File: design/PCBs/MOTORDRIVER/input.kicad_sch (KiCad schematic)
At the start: 2 parts, among them J1 Screw_Terminal_01x02, P3 USB_C_Plug_USB2.0

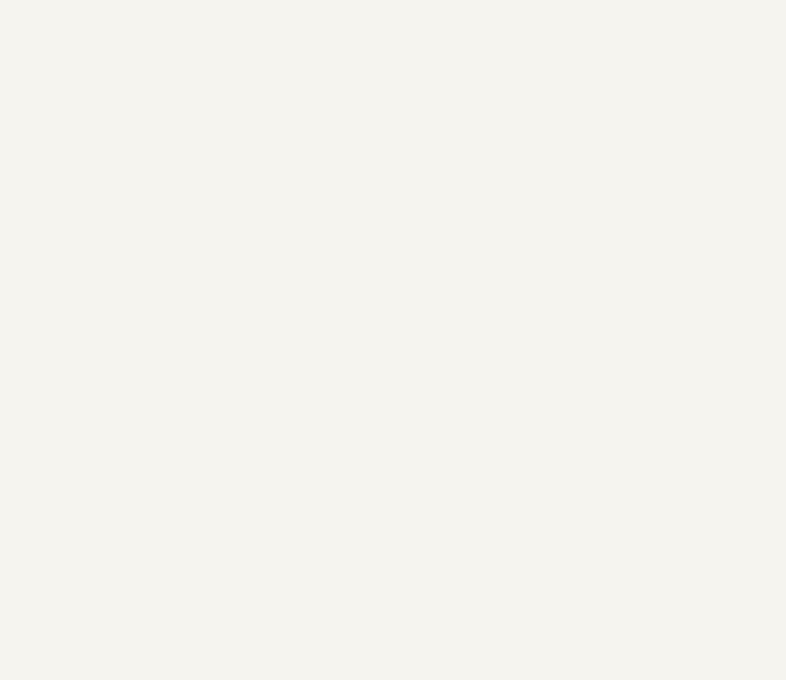
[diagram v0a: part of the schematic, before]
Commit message: Added micro-servo headers Added header for FFC cable IMU PCB
We need to set IMU PCB input to correspond to
the one we have made here.
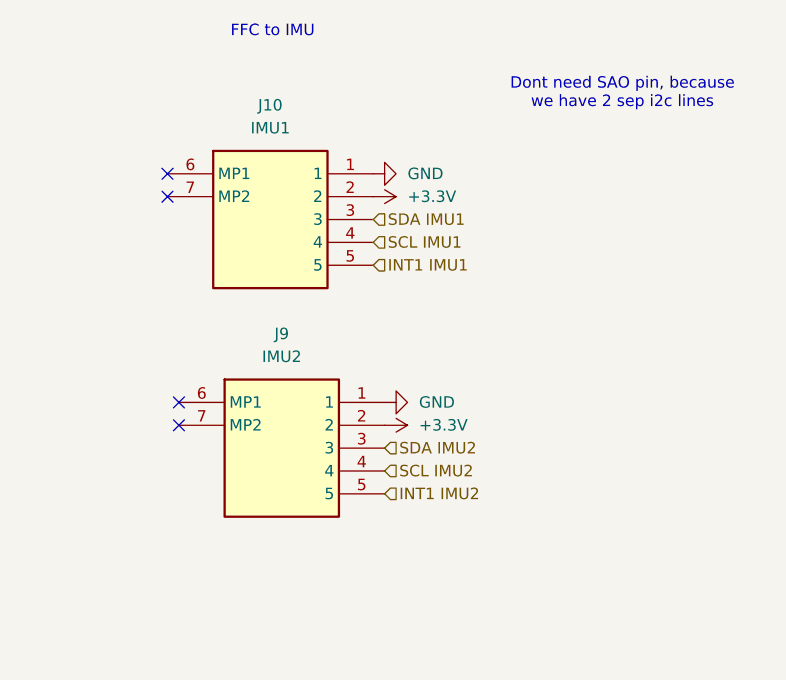
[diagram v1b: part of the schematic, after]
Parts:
- added J10: IMU1, 59453052110ECHLF, symbol 59453-052110ECHLF:59453-052110ECHLF
- added J9: IMU2, 59453052110ECHLF, symbol 59453-052110ECHLF:59453-052110ECHLF
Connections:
- net GND: now also J10.1, J9.1
- new net +3.3V: J10.2, J9.2
- new net INT1 IMU1: J10.5
- new net INT1 IMU2: J9.5
- new net SCL IMU1: J10.4
- new net SCL IMU2: J9.4
- new net SDA IMU1: J10.3
- new net SDA IMU2: J9.3
- no-connect marks 2 -> 6
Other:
- note added: "Dont need SAO pin, because we have 2 sep i2c lines"
- note added: "FFC to IMU"

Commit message: finished 12v voltage, The components for alost all ICs need values. Cleaned up a bit
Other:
- moved on the sheet: J1, J10, J9, P3

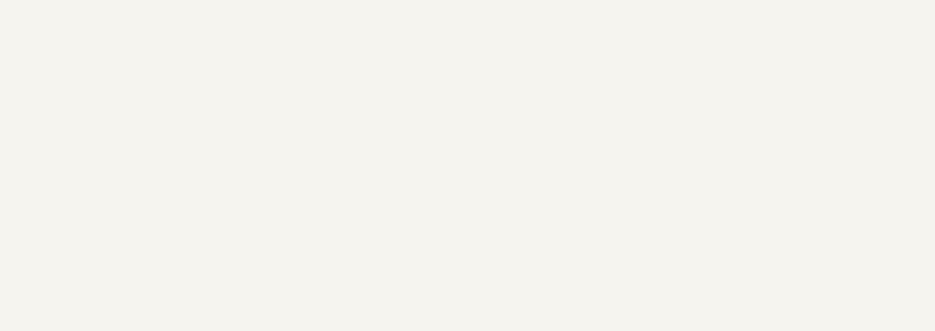
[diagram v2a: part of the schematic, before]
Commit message: documentation, values, double-checking stuff
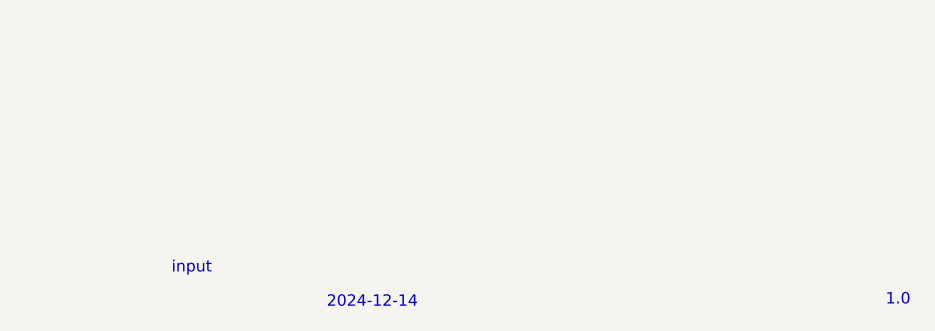
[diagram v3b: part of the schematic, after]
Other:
- note added: "1.0"
- note added: "2024-12-14"
- note added: "input"
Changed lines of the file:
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@@
 		(at 163.83 85.09)
+	)
+	(text "input\n"
+		(exclude_from_sim no)
+		(at 192.024 189.992 0)
+		(effects
+			(font
+				(size 1.27 1.27)
+			)
+		)
 	)
 	(text "Dont need SAO pin, because \nwe have 2 sep i2c lines"
@@
 		(effects
 			(font
+				(size 1.27 1.27)
+			)
+		)
+	)
+	(text "2024-12-14"
+		(exclude_from_sim no)
+		(at 212.09 193.802 0)
+		(effects
+			(font
+				(size 1.27 1.27)
+			)
+		)
+	)
+	(text "1.0"
+		(exclude_from_sim no)
+		(at 270.51 193.548 0)
+		(effects
+			(font

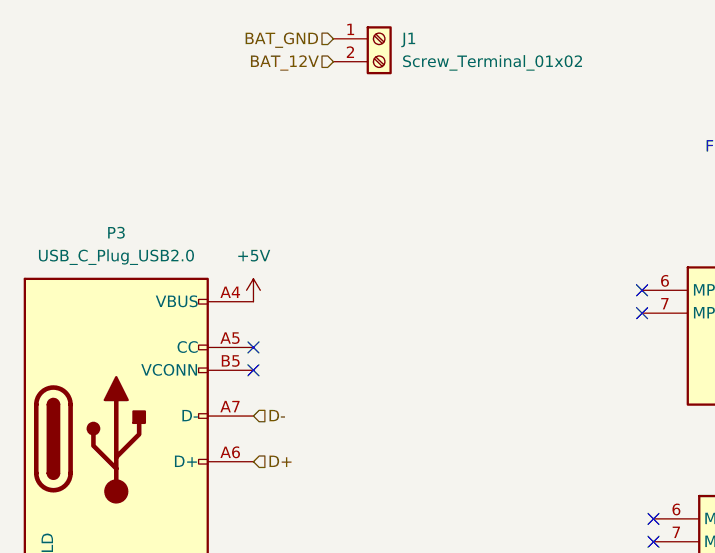
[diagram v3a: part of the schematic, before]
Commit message: component values for lm51
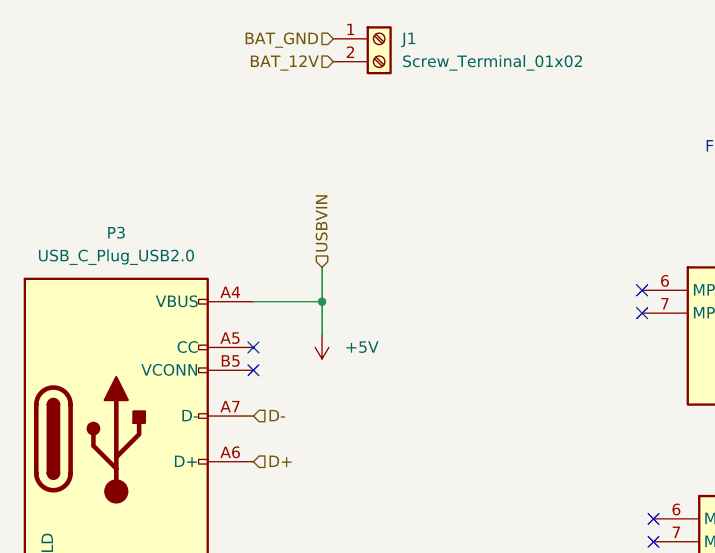
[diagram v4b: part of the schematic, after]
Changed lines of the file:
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@@
 	(generator_version "8.0")
 	(paper "A4")
+	(junction
+		(at 128.27 86.36)
+		(diameter 0)
+		(color 0 0 0 0)
+	)
 	(no_connect
 		(at 165.1 110.49)
@@
 		(at 163.83 85.09)
 	)
+	(wire
+		(pts
+			(xy 128.27 86.36) (xy 120.65 86.36)
+		)
+		(stroke
+			(width 0)
+			(type default)
+		)
+	)
+	(wire
+		(pts
+			(xy 128.27 90.17) (xy 128.27 86.36)
+		)
+		(stroke
+			(width 0)
+			(type default)
+		)
+	)
+	(wire
+		(pts
+			(xy 128.27 82.55) (xy 128.27 86.36)
+		)
+		(stroke
+			(width 0)
+			(type default)
+		)
+	)
 	(text "input\n"
 		(exclude_from_sim no)
@@
 		(shape input)
 		(at 120.65 99.06 0)
+		(fields_autoplaced yes)
+		(effects
+			(font
+				(size 1.27 1.27)
+			)
+			(justify left)
+		)
+	)
+	(hierarchical_label "USBVIN"
+		(shape input)
+		(at 128.27 82.55 90)
 		(fields_autoplaced yes)
 		(effects
@@
 	(symbol
 		(lib_id "power:+5V")
-		(at 120.65 86.36 0)
+		(at 128.27 90.17 180)
 		(unit 1)
 		(exclude_from_sim no)
@@
 		(fields_autoplaced yes)
 		(property "Reference" "#PWR089"
-			(at 120.65 90.17 0)
+			(at 128.27 86.36 0)
 			(effects
 				(font
@@
 		)
 		(property "Value" "+5V"
-			(at 120.65 81.28 0)
-			(effects
-				(font
-					(size 1.27 1.27)
-				)
+			(at 130.81 91.4399 0)
+			(effects
+				(font
+					(size 1.27 1.27)
+				)
+				(justify right)
 			)
 		)
 		(property "Footprint" ""
-			(at 120.65 86.36 0)
+			(at 128.27 90.17 0)
 			(effects
 				(font
@@
 		)
 		(property "Datasheet" ""
-			(at 120.65 86.36 0)
+			(at 128.27 90.17 0)
 			(effects
 				(font
@@
 		)
 		(property "Description" "Power symbol creates a global label with name \"+5V\""
-			(at 120.65 86.36 0)
-			(effects
-				(font
+			(at 128.27 90.17 0)
+			(effects
+				(font
